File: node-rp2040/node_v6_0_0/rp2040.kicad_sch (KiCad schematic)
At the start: 31 parts, among them SW1 PTS636 SM50J SMTR LFS, SW2 PTS636 SM50J SMTR LFS, SW3 PTS636 SM50J SMTR LFS, U1 RP2040, U14 W25Q128, U2 USBLC6-2SC6

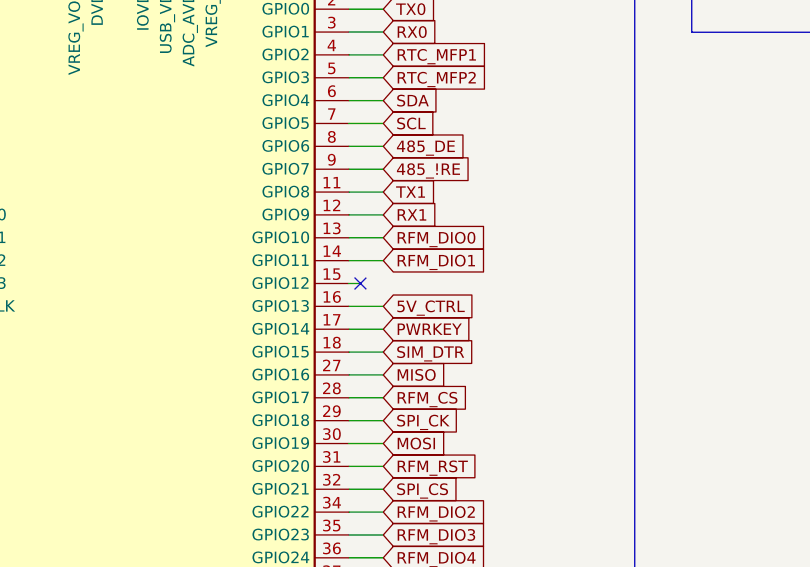
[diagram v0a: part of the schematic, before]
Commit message: i should have made this more than one commit but: 1) started poking around in v5 to find and solve a sim card problem, forgot about it and moved on 2) created v6, modified the schematic somewhat, removed some parts, began laying out the pcb again this time as a 6 layer board 3) fixed the library setup so now it uses symbols and footprints from the packages available alongside kicad (in void linux at least) for all standard stuff PLUS the wisdom libraries and the jlcpcb prefered parts library
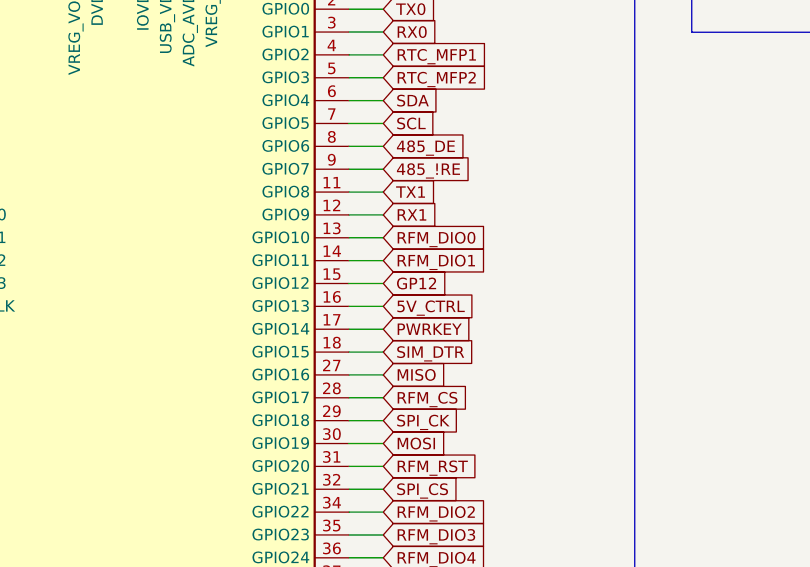
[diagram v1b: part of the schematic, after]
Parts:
- C1, C10, C11, C12, C19, C2, C20, C3, C4, C48, C5, C6, C7, C8: footprint JLCPCB-Kicad-Footprints:C_0402 -> JLCPCB:C_0402
- C13, C14, C15, C16, C47: footprint JLCPCB-Kicad-Footprints:C_0805 -> JLCPCB:C_0805
- R1, R2: footprint JLCPCB-Kicad-Footprints:R_0603 -> JLCPCB:R_0603
- R10, R5, R9: footprint JLCPCB-Kicad-Footprints:R_0805 -> JLCPCB:R_0805
- SW1, SW2, SW3: footprint WiSDOM:SW_PTS636_CNK -> pts636:SW_PTS636_CNK
- U1: footprint JLCPCB-Kicad-Footprints:QFN-56-1EP_7x7mm_P0.4mm_EP3.2x3.2mm_ThermalVias -> JLCPCB:QFN-56-1EP_7x7mm_P0.4mm_EP3.2x3.2mm_ThermalVias
- U14: footprint JLCPCB-Kicad-Footprints:SOIC-8_L5.3-W5.3-P1.27-LS8.0-BL -> JLCPCB:SOIC-8_L5.3-W5.3-P1.27-LS8.0-BL
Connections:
- net GP12: now reaches U1.15 (GPIO12)
- no-connect marks 1 -> 0
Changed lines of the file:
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@@
 		(color 0 0 0 0)
 	)
-	(no_connect
-		(at 90.17 123.19)
-	)
 	(wire
 		(pts
@@
 	(wire
 		(pts
-			(xy 88.9 123.19) (xy 90.17 123.19)
+			(xy 88.9 123.19) (xy 92.71 123.19)
 		)
 		(stroke
@@
 		)
 	)
+	(global_label "GP12"
+		(shape input)
+		(at 92.71 123.19 0)
+		(fields_autoplaced yes)
+		(effects
+			(font
+				(size 1.27 1.27)
+			)
+			(justify left)
+		)
+		(property "Intersheetrefs" "${INTERSHEET_REFS}"
+			(at 100.6542 123.19 0)
+			(effects
+				(font
+					(size 1.27 1.27)
+				)
+				(justify left)
+				(hide yes)
+			)
+		)
+	)
 	(global_label "USB+"
 		(shape input)
@@
 			)
 		)
-		(property "Footprint" "JLCPCB-Kicad-Footprints:R_0805"
+		(property "Footprint" "JLCPCB:R_0805"
 			(at 259.842 99.06 90)
 			(effects
@@
 			)
 		)
-		(property "Footprint" "JLCPCB-Kicad-Footprints:C_0402"
+		(property "Footprint" "JLCPCB:C_0402"
 			(at 51.562 30.48 90)
 			(effects
@@
 			)
 		)
-		(property "Footprint" "JLCPCB-Kicad-Footprints:C_0402"
+		(property "Footprint" "JLCPCB:C_0402"
 			(at 189.992 119.38 90)
 			(effects
@@
 			)
 		)
-		(property "Footprint" "JLCPCB-Kicad-Footprints:R_0603"
+		(property "Footprint" "JLCPCB:R_0603"
 			(at 30.48 101.092 90)
 			(effects
@@
 			)
 		)
-		(property "Footprint" "JLCPCB-Kicad-Footprints:C_0402"
+		(property "Footprint" "JLCPCB:C_0402"
 			(at 38.862 30.48 90)
 			(effects
@@
 			)
 		)
-		(property "Footprint" "JLCPCB-Kicad-Footprints:C_0402"
+		(property "Footprint" "JLCPCB:C_0402"
 			(at 200.66 66.548 90)
 			(effects
@@
 			)
 		)
-		(property "Footprint" "JLCPCB-Kicad-Footprints:C_0402"
+		(property "Footprint" "JLCPCB:C_0402"
 			(at 89.662 30.48 90)
 			(effects
@@
 			)
 		)
-		(property "Footprint" "JLCPCB-Kicad-Footprints:C_0402"
+		(property "Footprint" "JLCPCB:C_0402"
 			(at 200.66 79.248 90)
 			(effects
@@
 			)
 		)
-		(property "Footprint" "JLCPCB-Kicad-Footprints:R_0805"
+		(property "Footprint" "JLCPCB:R_0805"
 			(at 187.96 79.248 90)
 			(effects
@@
 			)
 		)
-		(property "Footprint" "JLCPCB-Kicad-Footprints:C_0805"
+		(property "Footprint" "JLCPCB:C_0805"
 			(at 177.292 119.38 90)
 			(effects
@@
 			)
 		)
-		(property "Footprint" "JLCPCB-Kicad-Footprints:C_0402"
+		(property "Footprint" "JLCPCB:C_0402"
 			(at 102.362 30.48 90)
 			(effects
@@
 			)
 		)
-		(property "Footprint" "JLCPCB-Kicad-Footprints:R_0603"
+		(property "Footprint" "JLCPCB:R_0603"
 			(at 30.48 98.552 90)
 			(effects
@@
 			)
 		)
-		(property "Footprint" "WiSDOM:SW_PTS636_CNK"
+		(property "Footprint" "pts636:SW_PTS636_CNK"
 			(at 242.824 90.17 0)
 			(effects
@@
 			)
 		)
-		(property "Footprint" "JLCPCB-Kicad-Footprints:QFN-56-1EP_7x7mm_P0.4mm_EP3.2x3.2mm_ThermalVias"
+		(property "Footprint" "JLCPCB:QFN-56-1EP_7x7mm_P0.4mm_EP3.2x3.2mm_ThermalVias"
 			(at 63.5 130.81 0)
 			(effects
@@
 			)
 		)
-		(property "Footprint" "JLCPCB-Kicad-Footprints:C_0402"
+		(property "Footprint" "JLCPCB:C_0402"
 			(at 188.722 33.02 90)
 			(effects
@@
 			)
 		)
-		(property "Footprint" "JLCPCB-Kicad-Footprints:C_0402"
+		(property "Footprint" "JLCPCB:C_0402"
 			(at 115.062 30.48 90)
 			(effects
@@
 			)
 		)
-		(property "Footprint" "JLCPCB-Kicad-Footprints:C_0805"
+		(property "Footprint" "JLCPCB:C_0805"
 			(at 229.362 33.02 90)
 			(effects
@@
 			)
 		)
-		(property "Footprint" "JLCPCB-Kicad-Footprints:R_0805"
+		(property "Footprint" "JLCPCB:R_0805"
 			(at 242.062 119.38 90)
 			(effects
@@
 			)
 		)
-		(property "Footprint" "JLCPCB-Kicad-Footprints:C_0805"
+		(property "Footprint" "JLCPCB:C_0805"
 			(at 150.622 30.48 90)
 			(effects
@@
 			)
 		)
-		(property "Footprint" "JLCPCB-Kicad-Footprints:SOIC-8_L5.3-W5.3-P1.27-LS8.0-BL"
+		(property "Footprint" "JLCPCB:SOIC-8_L5.3-W5.3-P1.27-LS8.0-BL"
 			(at 166.37 153.67 0)
 			(effects
@@
 			)
 		)
-		(property "Footprint" "JLCPCB-Kicad-Footprints:C_0805"
+		(property "Footprint" "JLCPCB:C_0805"
 			(at 137.922 30.48 90)
 			(effects
@@
 			)
 		)
-		(property "Footprint" "JLCPCB-Kicad-Footprints:C_0402"
+		(property "Footprint" "JLCPCB:C_0402"
 			(at 76.962 30.48 90)
 			(effects
@@
 			)
 		)
-		(property "Footprint" "JLCPCB-Kicad-Footprints:C_0402"
+		(property "Footprint" "JLCPCB:C_0402"
 			(at 176.022 33.02 90)
 			(effects
@@
 			)
 		)
-		(property "Footprint" "JLCPCB-Kicad-Footprints:C_0402"
+		(property "Footprint" "JLCPCB:C_0402"
 			(at 64.262 30.48 90)
 			(effects
@@
 			)
 		)
-		(property "Footprint" "WiSDOM:SW_PTS636_CNK"
+		(property "Footprint" "pts636:SW_PTS636_CNK"
 			(at 241.554 67.31 0)
 			(effects
@@
 			)
 		)
-		(property "Footprint" "JLCPCB-Kicad-Footprints:C_0402"
+		(property "Footprint" "JLCPCB:C_0402"
 			(at 26.162 30.48 90)
 			(effects
@@
 			)
 		)
-		(property "Footprint" "JLCPCB-Kicad-Footprints:C_0805"
+		(property "Footprint" "JLCPCB:C_0805"
 			(at 216.662 33.02 90)
 			(effects
@@
 			)
 		)
-		(property "Footprint" "WiSDOM:SW_PTS636_CNK"
+		(property "Footprint" "pts636:SW_PTS636_CNK"
 			(at 242.824 125.73 0)
 			(effects
@@
 			)
 		)
-		(property "Footprint" "JLCPCB-Kicad-Footprints:C_0402"
+		(property "Footprint" "JLCPCB:C_0402"
 			(at 201.422 33.02 90)
 			(effects
